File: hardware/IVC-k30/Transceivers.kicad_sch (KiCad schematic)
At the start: 7 parts, among them U10 74ABT16245DL, U11 74ABT16245DL, U12 74ABT16245DL, U17 74ABT16245DL, U6 74ABT16245DL, U8 74ABT16245DL, U9 74ABT16245DL

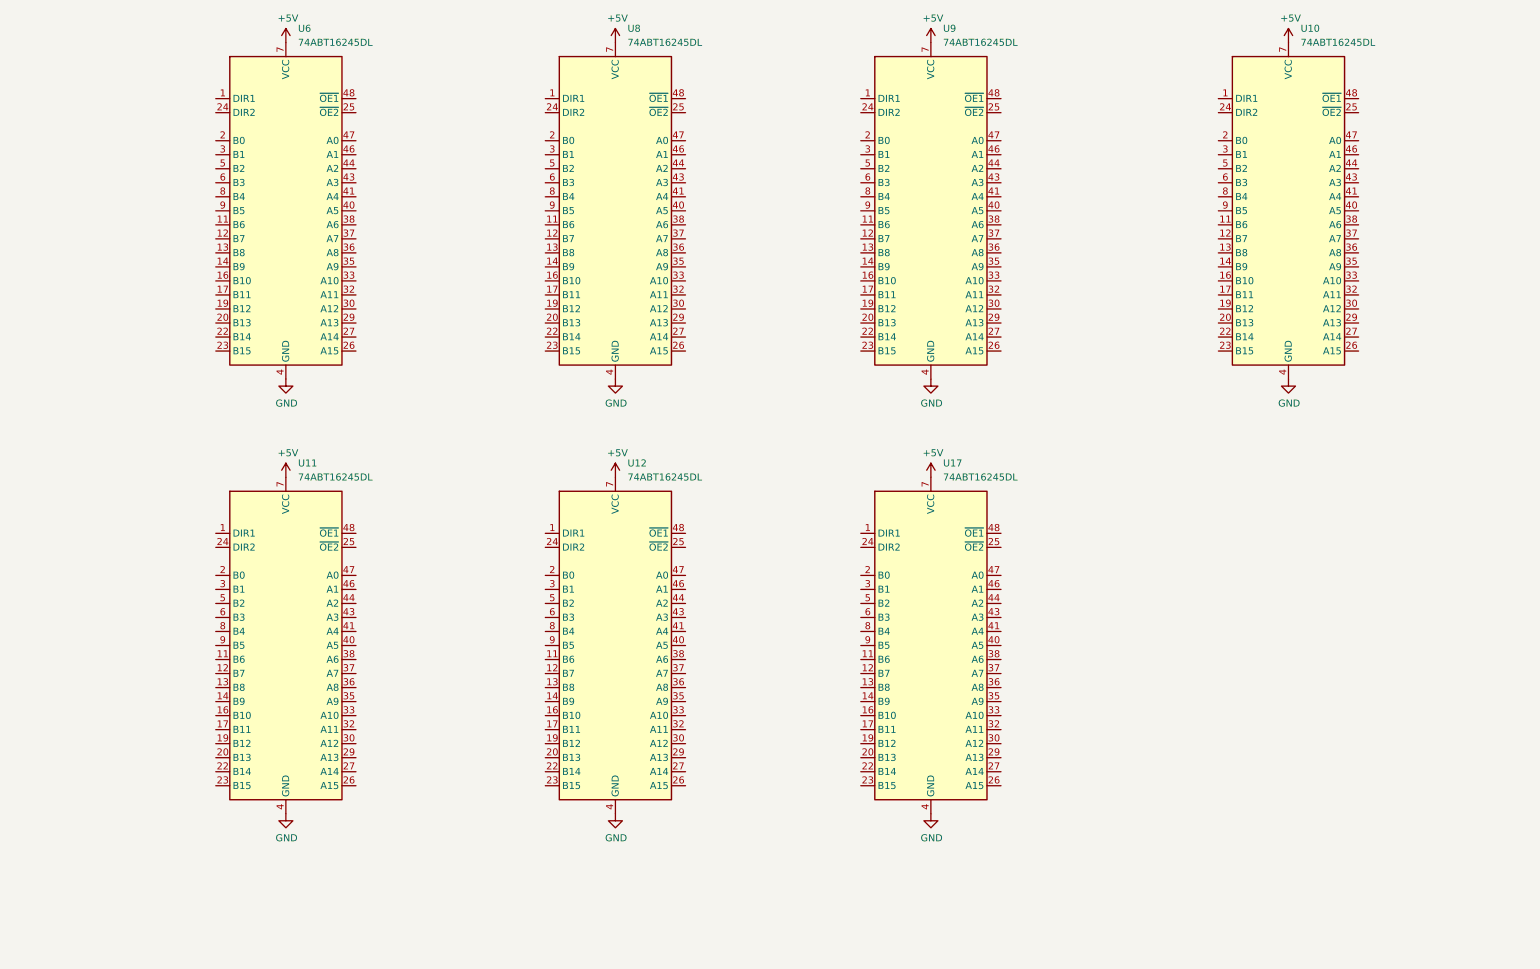
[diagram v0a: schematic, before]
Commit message: Updated k30 CPU card
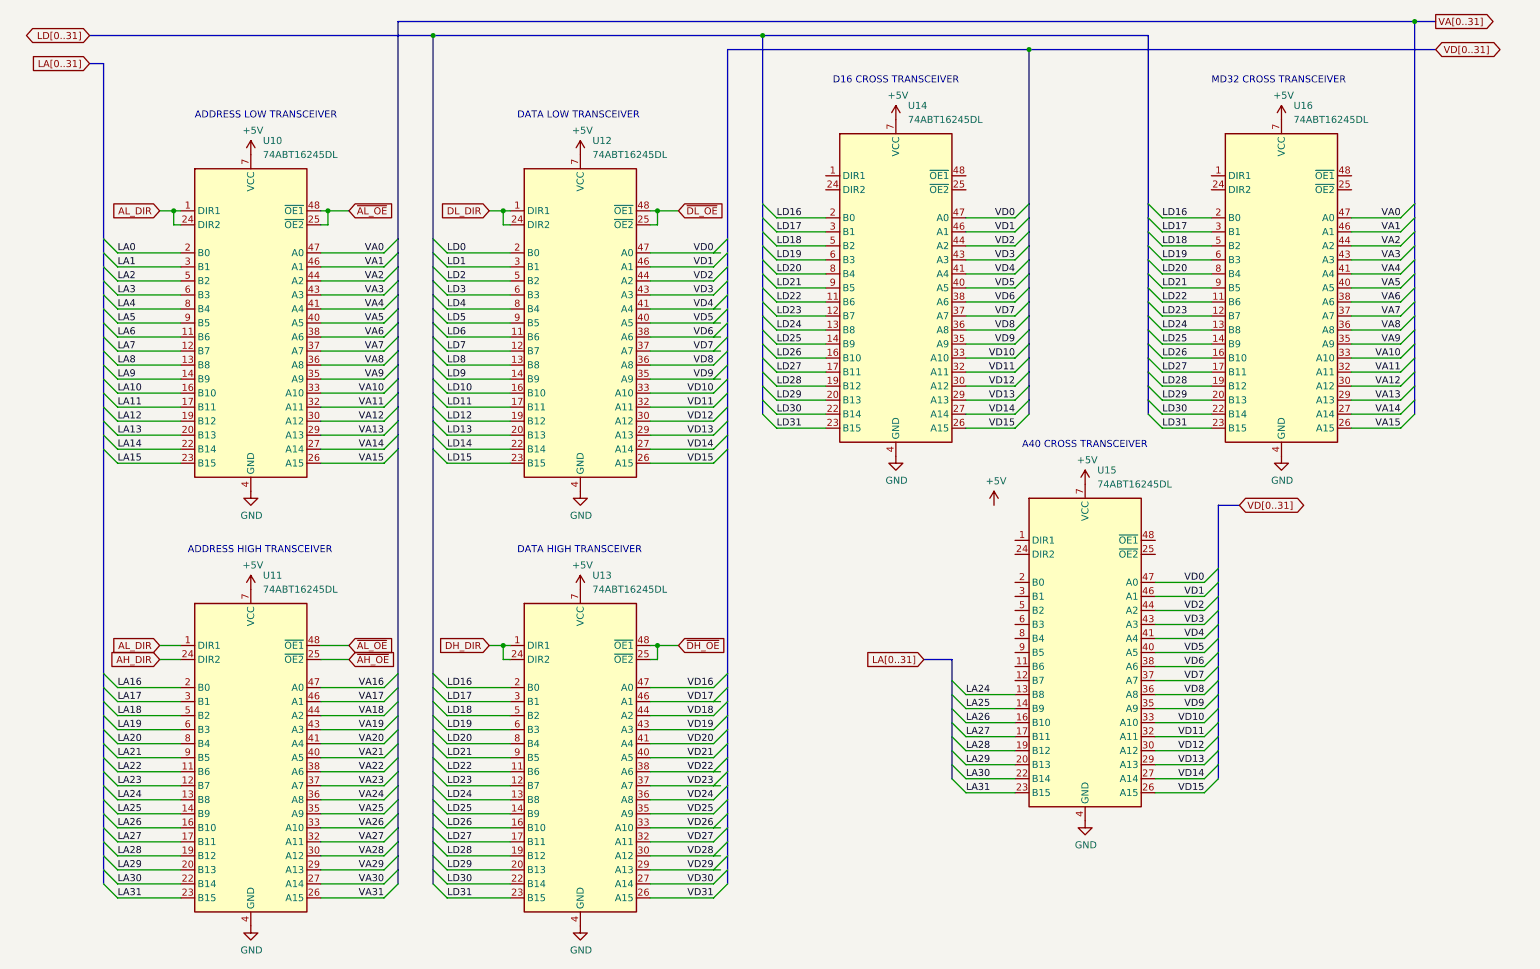
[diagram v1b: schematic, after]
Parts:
- renumbered U6 to U10, U8 to U12, U12 to U13, U9 to U14, U17 to U15, U10 to U16
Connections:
- net AL_DIR: now reaches U11.1 (DIR1)
- net AL_DIR: now also U10.1 (DIR1), U10.24 (DIR2)
- net LA22: now reaches U11.11 (B6)
- net LA23: now reaches U11.12 (B7)
- net LA24: now reaches U11.13 (B8)
- net LA24: now also U15.13 (B8)
- net LA25: now reaches U11.14 (B9)
- net LA25: now also U15.14 (B9)
- net LA26: now reaches U11.16 (B10)
- net LA26: now also U15.16 (B10)
- net LA27: now reaches U11.17 (B11)
- net LA27: now also U15.17 (B11)
- net LA28: now reaches U11.19 (B12)
- net LA28: now also U15.19 (B12)
- net LA16: now reaches U11.2 (B0)
- net LA29: now reaches U11.20 (B13)
- net LA29: now also U15.20 (B13)
- net LA30: now reaches U11.22 (B14)
- net LA30: now also U15.22 (B14)
- net LA31: now reaches U11.23 (B15)
- net LA31: now also U15.23 (B15)
- net AH_DIR: now reaches U11.24 (DIR2)
- net ~{AH_OE}: now reaches U11.25 (~{OE2})
- net VA31: now reaches U11.26 (A15)
- net VA30: now reaches U11.27 (A14)
- net VA29: now reaches U11.29 (A13)
- net LA17: now reaches U11.3 (B1)
- net VA28: now reaches U11.30 (A12)
- net VA27: now reaches U11.32 (A11)
- net VA26: now reaches U11.33 (A10)
- net VA25: now reaches U11.35 (A9)
- net VA24: now reaches U11.36 (A8)
- net VA23: now reaches U11.37 (A7)
- net VA22: now reaches U11.38 (A6)
- net VA21: now reaches U11.40 (A5)
- net VA20: now reaches U11.41 (A4)
- net VA19: now reaches U11.43 (A3)
- net VA18: now reaches U11.44 (A2)
- net VA17: now reaches U11.46 (A1)
- net VA16: now reaches U11.47 (A0)
- net ~{AL_OE}: now reaches U11.48 (~{OE1})
- net ~{AL_OE}: now also U10.25 (~{OE2}), U10.48 (~{OE1})
- net LA18: now reaches U11.5 (B2)
- net LA19: now reaches U11.6 (B3)
- net LA20: now reaches U11.8 (B4)
- net LA21: now reaches U11.9 (B5)
- net DL_DIR: now reaches U12.1 (DIR1)
- net DL_DIR: now also U12.24 (DIR2)
- net LD6: now reaches U12.11 (B6)
- net LD7: now reaches U12.12 (B7)
- net LD8: now reaches U12.13 (B8)
- net LD9: now reaches U12.14 (B9)
- net LD10: now reaches U12.16 (B10)
- net LD11: now reaches U12.17 (B11)
- net LD12: now reaches U12.19 (B12)
- net LD0: now reaches U12.2 (B0)
- net LD13: now reaches U12.20 (B13)
- net LD14: now reaches U12.22 (B14)
- net LD15: now reaches U12.23 (B15)
- net ~{DL_OE}: now reaches U12.25 (~{OE2})
- net ~{DL_OE}: now also U12.48 (~{OE1})
- net VD15: now reaches U12.26 (A15)
- net VD15: now also U14.26 (A15), U15.26 (A15)
- net VD14: now reaches U12.27 (A14)
- net VD14: now also U14.27 (A14), U15.27 (A14)
- net VD13: now reaches U12.29 (A13)
- net VD13: now also U14.29 (A13), U15.29 (A13)
- net LD1: now reaches U12.3 (B1)
- net VD12: now reaches U12.30 (A12)
- net VD12: now also U14.30 (A12), U15.30 (A12)
- net VD11: now reaches U12.32 (A11)
- net VD11: now also U14.32 (A11), U15.32 (A11)
- net VD10: now reaches U12.33 (A10)
- net VD10: now also U14.33 (A10), U15.33 (A10)
- net VD9: now reaches U12.35 (A9)
- net VD9: now also U14.35 (A9), U15.35 (A9)
- net VD8: now reaches U12.36 (A8)
- net VD8: now also U14.36 (A8), U15.36 (A8)
- net VD7: now reaches U12.37 (A7)
- net VD7: now also U14.37 (A7), U15.37 (A7)
- net VD6: now reaches U12.38 (A6)
- net VD6: now also U14.38 (A6), U15.38 (A6)
- net VD5: now reaches U12.40 (A5)
- net VD5: now also U14.40 (A5), U15.40 (A5)
- net VD4: now reaches U12.41 (A4)
- net VD4: now also U14.41 (A4), U15.41 (A4)
- net VD3: now reaches U12.43 (A3)
- net VD3: now also U14.43 (A3), U15.43 (A3)
- net VD2: now reaches U12.44 (A2)
- net VD2: now also U14.44 (A2), U15.44 (A2)
- net VD1: now reaches U12.46 (A1)
- net VD1: now also U14.46 (A1), U15.46 (A1)
- net VD0: now reaches U12.47 (A0)
- net VD0: now also U14.47 (A0), U15.47 (A0)
- net LD2: now reaches U12.5 (B2)
- net LD3: now reaches U12.6 (B3)
- net LD4: now reaches U12.8 (B4)
- net LD5: now reaches U12.9 (B5)
- net LA6: now reaches U10.11 (B6)
- net LA7: now reaches U10.12 (B7)
- net LA8: now reaches U10.13 (B8)
- net LA9: now reaches U10.14 (B9)
- net LA10: now reaches U10.16 (B10)
- net LA11: now reaches U10.17 (B11)
- net LA12: now reaches U10.19 (B12)
- net LA0: now reaches U10.2 (B0)
- net LA13: now reaches U10.20 (B13)
- net LA14: now reaches U10.22 (B14)
- net LA15: now reaches U10.23 (B15)
- net VA15: now reaches U10.26 (A15)
- net VA15: now also U16.26 (A15)
- net VA14: now reaches U10.27 (A14)
- net VA14: now also U16.27 (A14)
- net VA13: now reaches U10.29 (A13)
- net VA13: now also U16.29 (A13)
- net LA1: now reaches U10.3 (B1)
- net VA12: now reaches U10.30 (A12)
- net VA12: now also U16.30 (A12)
- net VA11: now reaches U10.32 (A11)
- net VA11: now also U16.32 (A11)
- net VA10: now reaches U10.33 (A10)
- net VA10: now also U16.33 (A10)
- net VA9: now reaches U10.35 (A9)
- net VA9: now also U16.35 (A9)
- net VA8: now reaches U10.36 (A8)
- net VA8: now also U16.36 (A8)
- net VA7: now reaches U10.37 (A7)
- net VA7: now also U16.37 (A7)
- net VA6: now reaches U10.38 (A6)
- net VA6: now also U16.38 (A6)
- net VA5: now reaches U10.40 (A5)
- net VA5: now also U16.40 (A5)
- net VA4: now reaches U10.41 (A4)
- net VA4: now also U16.41 (A4)
- net VA3: now reaches U10.43 (A3)
- net VA3: now also U16.43 (A3)
- net VA2: now reaches U10.44 (A2)
- net VA2: now also U16.44 (A2)
- net VA1: now reaches U10.46 (A1)
- net VA1: now also U16.46 (A1)
- net VA0: now reaches U10.47 (A0)
- net VA0: now also U16.47 (A0)
- net LA2: now reaches U10.5 (B2)
- net LA3: now reaches U10.6 (B3)
- net LA4: now reaches U10.8 (B4)
- net LA5: now reaches U10.9 (B5)
- net DH_DIR: now reaches U13.1 (DIR1)
- net DH_DIR: now also U13.24 (DIR2)
- net LD22: now reaches U13.11 (B6)
- net LD22: now also U14.11 (B6), U16.11 (B6)
- net LD23: now reaches U13.12 (B7)
- net LD23: now also U14.12 (B7), U16.12 (B7)
- net LD24: now reaches U13.13 (B8)
- net LD24: now also U14.13 (B8), U16.13 (B8)
- net LD25: now reaches U13.14 (B9)
- net LD25: now also U14.14 (B9), U16.14 (B9)
- net LD26: now reaches U13.16 (B10)
- net LD26: now also U14.16 (B10), U16.16 (B10)
- net LD27: now reaches U13.17 (B11)
- net LD27: now also U14.17 (B11), U16.17 (B11)
- net LD28: now reaches U13.19 (B12)
- net LD28: now also U14.19 (B12), U16.19 (B12)
- net LD16: now reaches U13.2 (B0)
- net LD16: now also U14.2 (B0), U16.2 (B0)
- net LD29: now reaches U13.20 (B13)
- net LD29: now also U14.20 (B13), U16.20 (B13)
- net LD30: now reaches U13.22 (B14)
- net LD30: now also U14.22 (B14), U16.22 (B14)
- net LD31: now reaches U13.23 (B15)
- net LD31: now also U14.23 (B15), U16.23 (B15)
- net ~{DH_OE}: now reaches U13.25 (~{OE2})
- net ~{DH_OE}: now also U13.48 (~{OE1})
- net VD31: now reaches U13.26 (A15)
- net VD30: now reaches U13.27 (A14)
- net VD29: now reaches U13.29 (A13)
- net LD17: now reaches U13.3 (B1)
- net LD17: now also U14.3 (B1), U16.3 (B1)
- net VD28: now reaches U13.30 (A12)
- net VD27: now reaches U13.32 (A11)
- net VD26: now reaches U13.33 (A10)
- net VD25: now reaches U13.35 (A9)
- net VD24: now reaches U13.36 (A8)
- net VD23: now reaches U13.37 (A7)
- net VD22: now reaches U13.38 (A6)
- net VD21: now reaches U13.40 (A5)
- net VD20: now reaches U13.41 (A4)
- net VD19: now reaches U13.43 (A3)
- net VD18: now reaches U13.44 (A2)
- net VD17: now reaches U13.46 (A1)
- net VD16: now reaches U13.47 (A0)
- net LD18: now reaches U13.5 (B2)
- net LD18: now also U14.5 (B2), U16.5 (B2)
- net LD19: now reaches U13.6 (B3)
- net LD19: now also U14.6 (B3), U16.6 (B3)
- net LD20: now reaches U13.8 (B4)
- net LD20: now also U14.8 (B4), U16.8 (B4)
- net LD21: now reaches U13.9 (B5)
- net LD21: now also U14.9 (B5), U16.9 (B5)
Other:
- note added: "A40 CROSS TRANSCEIVER"
- note added: "ADDRESS HIGH TRANSCEIVER"
- note added: "ADDRESS LOW TRANSCEIVER"
- note added: "D16 CROSS TRANSCEIVER"
- note added: "DATA HIGH TRANSCEIVER"
- note added: "DATA LOW TRANSCEIVER"
- note added: "MD32 CROSS TRANSCEIVER"
- title: (none) -> IVC-k30
- moved on the sheet: U10, U11, U12, U13, U14, U15, U16

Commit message: Committed changes to k30 board from Oct 9th 2023
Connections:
- net +5V: now also U15.11 (B6), U15.12 (B7), U15.2 (B0), U15.3 (B1), U15.5 (B2), U15.6 (B3), U15.8 (B4), U15.9 (B5)
- net MD32X_DIR: now reaches U16.1 (DIR1)
- net MD32X_DIR: now also U16.24 (DIR2)
- net ~{MD32X_OE}: now reaches U16.25 (~{OE2})
- net ~{MD32X_OE}: now also U16.48 (~{OE1})
- net A40X_DIR: now reaches U15.1 (DIR1)
- net A40X_DIR: now also U15.24 (DIR2)
- net ~{A40X_OE}: now reaches U15.25 (~{OE2})
- net ~{A40X_OE}: now also U15.48 (~{OE1})
- net D16X_DIR: now reaches U14.1 (DIR1)
- net D16X_DIR: now also U14.24 (DIR2)
- net ~{D16X_OE}: now reaches U14.25 (~{OE2})
- net ~{D16X_OE}: now also U14.48 (~{OE1})
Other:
- moved on the sheet: U14, U16
